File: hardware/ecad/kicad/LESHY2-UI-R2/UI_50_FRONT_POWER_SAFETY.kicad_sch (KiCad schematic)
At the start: 36 parts, among them Q6 Diodes Incorporated 2N7002DW-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, U50 LTC5532ES6#TRMPBF, U51 VEMD1060X01, U52 LTC5532ES6#TRMPBF, U53 TLV1824PWR, U54 TLV1824PWR, U55 TLV9061IDBVR, U56 SN74LVC1G07DCKR, U57 Texas Instruments SN74LVC1G06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, U58 SN74LVC08APWR

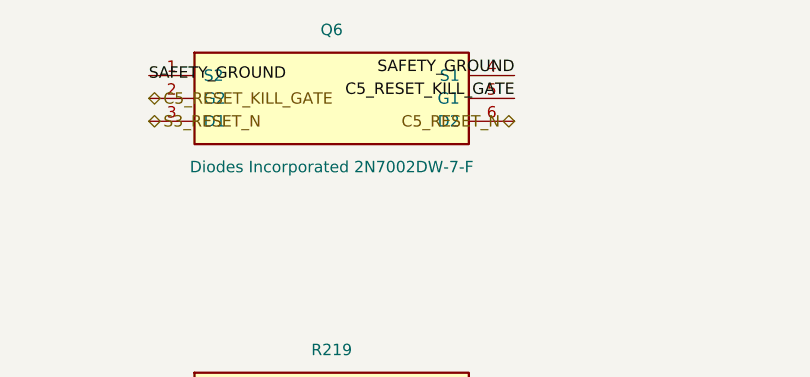
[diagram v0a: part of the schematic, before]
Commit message: Review R2 startup and fault-display sequencing
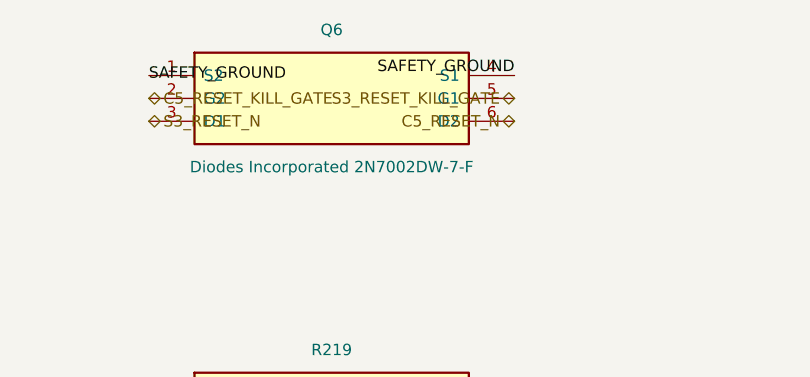
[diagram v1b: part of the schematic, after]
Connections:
- net C5_RESET_KILL_GATE: no longer Q6.5 (G1)
- new net S3_RESET_KILL_GATE: Q6.5 (G1)
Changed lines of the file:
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@@
 		(effects (font (size 1.27 1.27)) (justify right bottom))
 	)
-	(label "C5_RESET_KILL_GATE"
+	(hierarchical_label "S3_RESET_KILL_GATE"
+		(shape bidirectional)
 		(at 624.84 52.07 180)
 		(effects (font (size 1.27 1.27)) (justify right bottom))

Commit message: Canonicalize physical ground anchors
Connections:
- net SAFETY_GROUND renamed POWER_GROUND
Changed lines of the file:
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@@
 		(effects (font (size 1.27 1.27)))
 	)
-	(hierarchical_label "SAFETY_GROUND"
+	(hierarchical_label "POWER_GROUND"
 		(shape bidirectional)
 		(at 76.20 50.80 180)
@@
 		(effects (font (size 1.27 1.27)))
 	)
-	(label "SAFETY_GROUND"
+	(label "POWER_GROUND"
 		(at 167.64 50.80 180)
 		(effects (font (size 1.27 1.27)) (justify right bottom))
@@
 		(effects (font (size 1.27 1.27)))
 	)
-	(label "SAFETY_GROUND"
+	(label "POWER_GROUND"
 		(at 350.52 50.80 180)
 		(effects (font (size 1.27 1.27)) (justify right bottom))
@@
 		(effects (font (size 1.27 1.27)))
 	)
-	(label "SAFETY_GROUND"
+	(label "POWER_GROUND"
 		(at 441.96 50.80 180)
 		(effects (font (size 1.27 1.27)) (justify right bottom))
@@
 		(effects (font (size 1.27 1.27)))
 	)
-	(label "SAFETY_GROUND"
+	(label "POWER_GROUND"
 		(at 533.40 50.80 180)
 		(effects (font (size 1.27 1.27)) (justify right bottom))
@@
 		)
 	)
-	(label "SAFETY_GROUND"
+	(label "POWER_GROUND"
 		(at 584.20 49.53 0)
 		(effects (font (size 1.27 1.27)))
@@
 		(effects (font (size 1.27 1.27)))
 	)
-	(label "SAFETY_GROUND"
+	(label "POWER_GROUND"
 		(at 624.84 49.53 180)
 		(effects (font (size 1.27 1.27)) (justify right bottom))
@@
 		(effects (font (size 1.27 1.27)))
 	)
-	(label "SAFETY_GROUND"
+	(label "POWER_GROUND"
 		(at 899.16 50.80 180)
 		(effects (font (size 1.27 1.27)) (justify right bottom))
@@
 		(effects (font (size 1.27 1.27)))
 	)
-	(label "SAFETY_GROUND"
+	(label "POWER_GROUND"
 		(at 259.08 86.36 180)
 		(effects (font (size 1.27 1.27)) (justify right bottom))
@@
 		(effects (font (size 1.27 1.27)))
 	)
-	(label "SAFETY_GROUND"
+	(label "POWER_GROUND"
 		(at 624.84 86.36 180)
 		(effects (font (size 1.27 1.27)) (justify right bottom))
@@
 		(effects (font (size 1.27 1.27)))
 	)
-	(label "SAFETY_GROUND"
+	(label "POWER_GROUND"
 		(at 990.60 86.36 180)
 		(effects (font (size 1.27 1.27)) (justify right bottom))
@@
 		(effects (font (size 1.27 1.27)))
 	)
-	(label "SAFETY_GROUND"
+	(label "POWER_GROUND"
 		(at 309.88 123.19 0)
 		(effects (font (size 1.27 1.27)))
 	)
-	(label "SAFETY_GROUND"
+	(label "POWER_GROUND"
 		(at 309.88 125.73 0)
 		(effects (font (size 1.27 1.27)))
@@
 		)
 	)
-	(label "SAFETY_GROUND"
+	(label "POWER_GROUND"
 		(at 401.32 121.92 0)
 		(effects (font (size 1.27 1.27)))
@@
 		(effects (font (size 1.27 1.27)))
 	)
-	(label "SAFETY_GROUND"
+	(label "POWER_GROUND"
 		(at 492.76 123.19 0)
 		(effects (font (size 1.27 1.27)))
 	)
-	(label "SAFETY_GROUND"
+	(label "POWER_GROUND"
 		(at 492.76 125.73 0)
 		(effects (font (size 1.27 1.27)))
@@
 		(effects (font (size 1.27 1.27)) (justify right bottom))
 	)
-	(label "SAFETY_GROUND"
+	(label "POWER_GROUND"
 		(at 624.84 124.46 180)
 		(effects (font (size 1.27 1.27)) (justify right bottom))
 	)
-	(label "SAFETY_GROUND"
+	(label "POWER_GROUND"
 		(at 624.84 127.00 180)
 		(effects (font (size 1.27 1.27)) (justify right bottom))
 	)
-	(label "SAFETY_GROUND"
+	(label "POWER_GROUND"
 		(at 624.84 129.54 180)
 		(effects (font (size 1.27 1.27)) (justify right bottom))
@@
 		(effects (font (size 1.27 1.27)) (justify right bottom))
 	)
-	(label "SAFETY_GROUND"
+	(label "POWER_GROUND"
 		(at 716.28 124.46 180)
 		(effects (font (size 1.27 1.27)) (justify right bottom))
 	)
-	(label "SAFETY_GROUND"
+	(label "POWER_GROUND"
 		(at 716.28 127.00 180)
 		(effects (font (size 1.27 1.27)) (justify right bottom))
 	)
-	(label "SAFETY_GROUND"
+	(label "POWER_GROUND"
 		(at 716.28 129.54 180)
 		(effects (font (size 1.27 1.27)) (justify right bottom))
@@
 		(effects (font (size 1.27 1.27)))
 	)
-	(label "SAFETY_GROUND"
+	(label "POWER_GROUND"
 		(at 767.08 123.19 0)
 		(effects (font (size 1.27 1.27)))
@@
 		(effects (font (size 1.27 1.27)))
 	)
-	(label "SAFETY_GROUND"
+	(label "POWER_GROUND"
 		(at 858.52 125.73 0)
 		(effects (font (size 1.27 1.27)))
@@
 		(effects (font (size 1.27 1.27)))
 	)
-	(label "SAFETY_GROUND"
+	(label "POWER_GROUND"
 		(at 949.96 125.73 0)
 		(effects (font (size 1.27 1.27)))
@@
 		(effects (font (size 1.27 1.27)))
 	)
-	(label "SAFETY_GROUND"
+	(label "POWER_GROUND"
 		(at 1041.40 134.62 0)
 		(effects (font (size 1.27 1.27)))

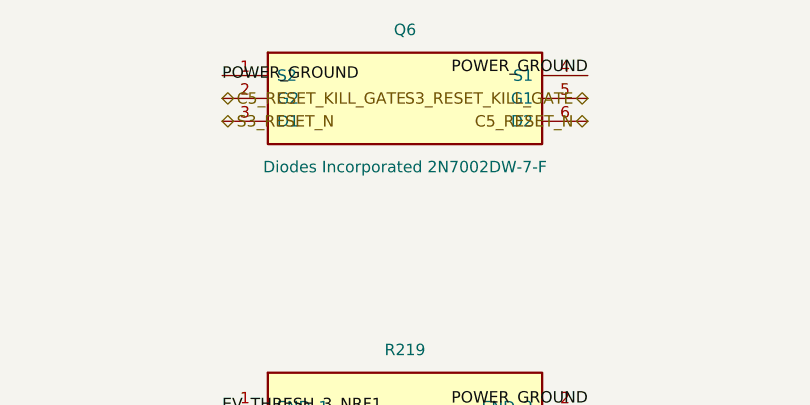
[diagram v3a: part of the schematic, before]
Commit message: Repair C5 service mux controls without weakening hardware KILL
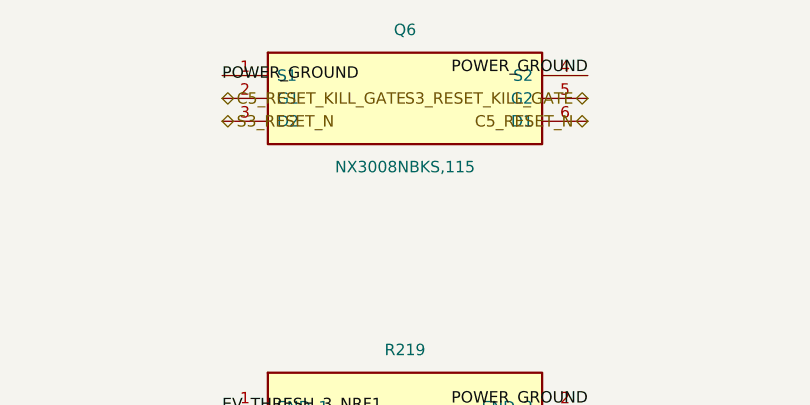
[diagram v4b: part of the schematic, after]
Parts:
- Q6: value Diodes Incorporated 2N7002DW-7-F -> NX3008NBKS,115; symbol Leshy2_R2:diodes_2n7002dw_7_f -> Leshy2_R2:nexperia_nx3008nbks_115
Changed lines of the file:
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@@
 	)
 	(symbol
-		(lib_id "Leshy2_R2:diodes_2n7002dw_7_f")
+		(lib_id "Leshy2_R2:nexperia_nx3008nbks_115")
 		(at 604.52 52.07 0)
 		(unit 1)
@@
 			(effects (font (size 1.27 1.27)))
 		)
-		(property "Value" "Diodes Incorporated 2N7002DW-7-F"
+		(property "Value" "NX3008NBKS,115"
 			(at 604.52 59.69 0)
 			(show_name no)
@@
 			(effects (font (size 1.27 1.27)))
 		)
-		(property "Description" "diodes_2n7002dw_7_f"
+		(property "Description" "nexperia_nx3008nbks_115"
 			(at 604.52 52.07 0)
 			(show_name no)
